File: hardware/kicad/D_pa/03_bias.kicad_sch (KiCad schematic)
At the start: 36 parts, among them U20 MCP4922-E/SL, U21 MCP4922-E/SL, U31 INA240A1DR, U32 INA240A1DR, U33 INA240A1DR, U34 INA240A1DR, U41 LM358, U42 LM358

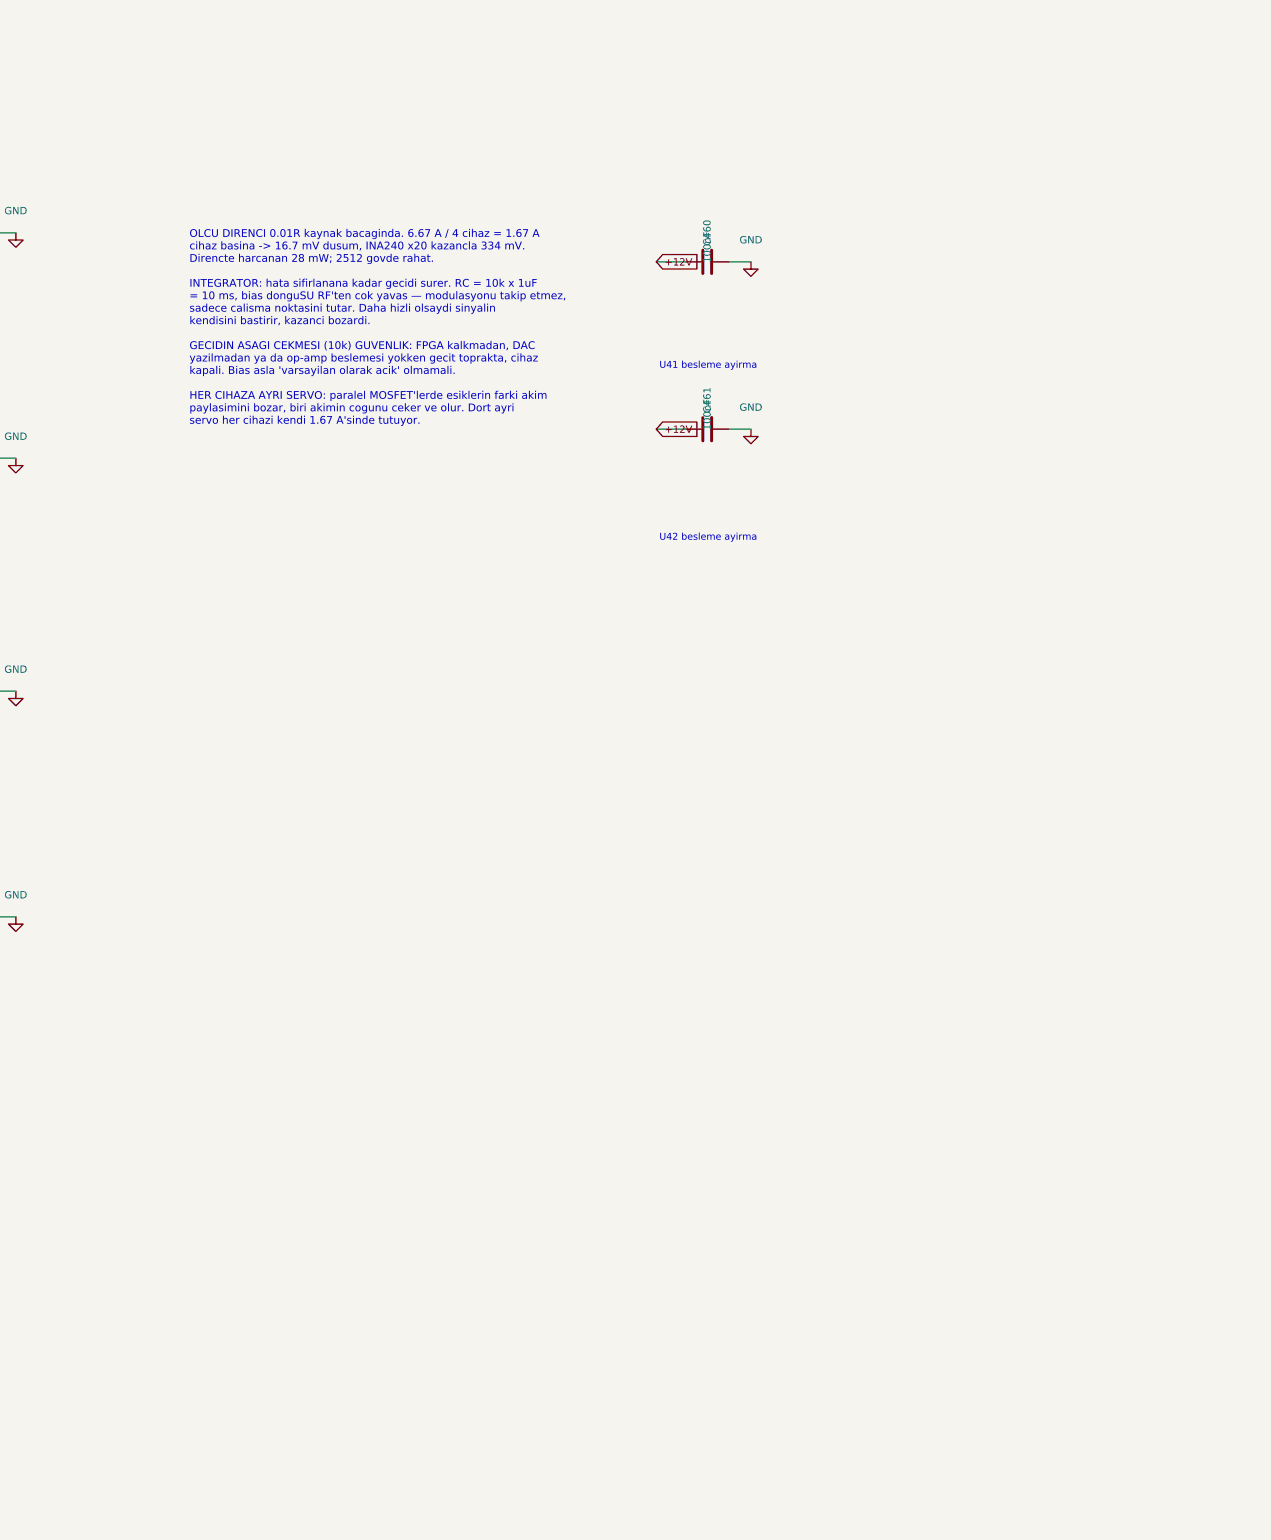
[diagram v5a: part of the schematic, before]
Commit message: Add BIAS_KILL to remove a single-fault destruction path
Each final device has its own closed-loop bias servo: a 0.01 ohm
sense resistor, an INA240A1 with a gain of 20, an LM358 integrator,
and the gate. Separate servos are correct for paralleled MOSFETs,
because different threshold voltages make one device take most of the
current.

A new tool measures the loop in ngspice. It does not model the inside
of the MOSFET. The boundary conditions are sufficient: input
capacitance, transconductance and threshold voltage.

The loop is stable. The crossover is at 25.7 Hz, the phase margin is
90 degrees, and the current reaches the set value in 106 ms.

The failure behaviour is destructive. The integrator raises the gate
until the measured current equals the set value. If the measurement
arm opens, the measured current reads zero. The error never closes.

  the gate reaches 10.4 V in 285 ms
  57.6 A and 2878 W in each device
  the continuous limit of the IRFP250N is 214 W

All four devices fail. The protection circuit kills what it protects.

A zener clamp does not solve this. The transconductance is 8 S, so
1 V above the threshold already gives 8 A. A safe clamp voltage would
be too near the operating point.

The board sees the condition already. Board 06 says: if the quiescent
current differs from the set value by 20 percent, the bias servo is
faulty, so cut. But PA_INHIBIT removes only the driver supply. In a
class-A stage the quiescent current does the damage, not the drive.

BIAS_KILL short-circuits the integrator capacitor. A pull-down on the
gate alone is not sufficient: the integrator would stay charged at
the rail, and the gate would jump to 10.5 V when the fault clears.
With the capacitor short-circuited, the op-amp follows the set
voltage and the gate stays at 0.33 V. The threshold is 3.2 V.

The circuit is one 2N7002 that inverts PA_INHIBIT, a 10k pull-up, and
one 2N7002 across each integrator capacitor. The unpowered state is
safe: the 10k pull-downs hold the gate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
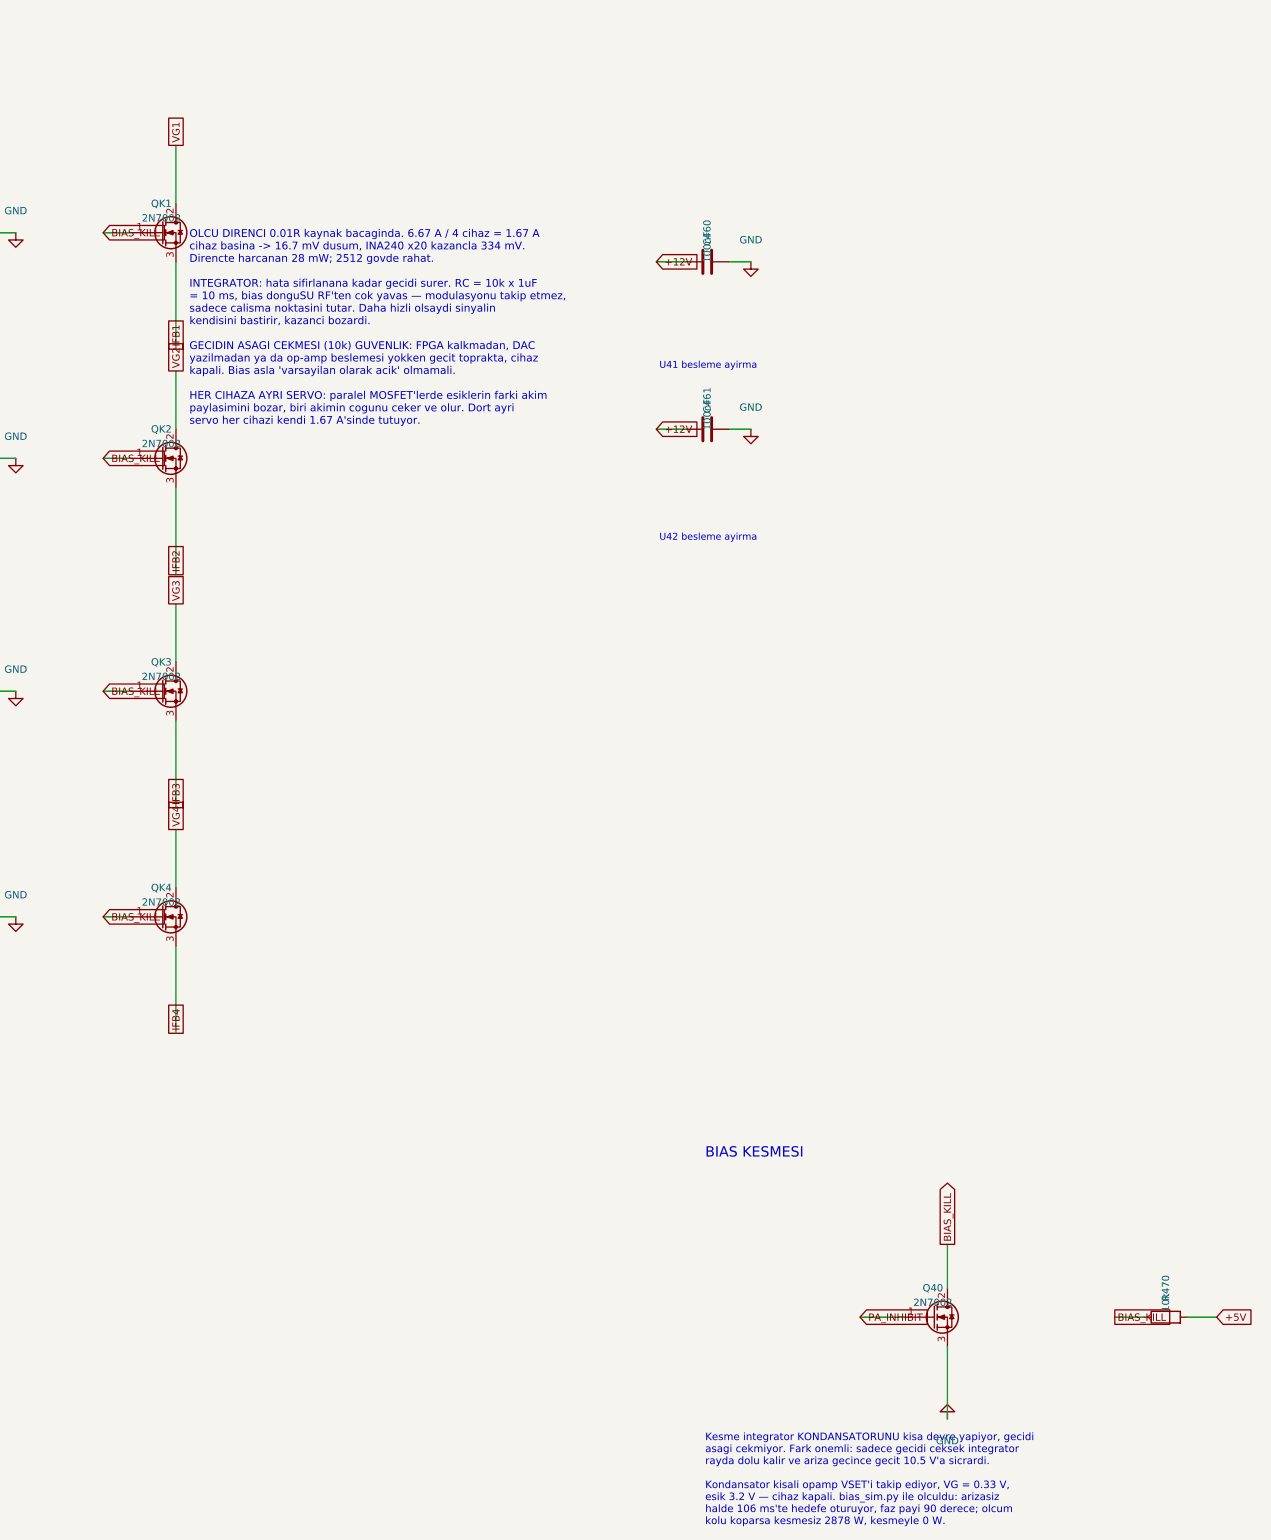
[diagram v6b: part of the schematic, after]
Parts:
- added Q40, QK1, QK2, QK3, QK4: 2N7002, Package_TO_SOT_SMD:SOT-23, symbol Transistor_FET:Q_NMOS_GDS
- added R470: 10k, Resistor_SMD:R_0603_1608Metric, symbol Device:R
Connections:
- net +5V: now also R470.2
- net GND: now also Q40.3 (S)
- net IFB1: now also QK1.3 (S)
- net IFB2: now also QK2.3 (S)
- net IFB3: now also QK3.3 (S)
- net IFB4: now also QK4.3 (S)
- net VG1: now also QK1.2 (D)
- net VG2: now also QK2.2 (D)
- net VG3: now also QK3.2 (D)
- net VG4: now also QK4.2 (D)
- new net BIAS_KILL: Q40.2 (D), QK1.1 (G), QK2.1 (G), QK3.1 (G), QK4.1 (G), R470.1
- new net PA_INHIBIT: Q40.1 (G)
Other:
- note added: "BIAS KESMESI"
- note added: "Kesme integrator KONDANSATORUNU kisa devre yapiyor, gecidi asagi cekmiyor. Fark onemli: sadece gecidi ceksek integrator rayda dolu kalir ve ariza gecince gecit 10.5 V'a sicrardi. Kondansator kisali opamp VSET'i takip ediyor, VG = 0.33 V, esik 3.2 V — cihaz kapali. bias_sim.py ile olculdu: arizasiz halde 106 ms'te hedefe oturuyor, faz payi 90 derece; olcum kolu koparsa kesmesiz 2878 W, kesmeyle 0 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"
